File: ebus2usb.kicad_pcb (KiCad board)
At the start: 2 copper layers, 86.8 x 30.4 mm, 42 parts, among them J1 MKDSN1,5/2-5,08, J2 Molex 53047-0210, J3 Molex 53047-0410, J4 Molex 53047-0210, J5 Molex 53047-0410, J6 Molex 67068-8000, Q1 BC817-40, Q2 BC817-40, U1 TS3702, U2 ADuM1201, U3 CH340N

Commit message: v0.8.1 * Size of main board changed to 87mm x 14.8mm * R5 changed from 1K5 to 4K7 * TS3702/TCL3702 replaced by TSX3702 (need VCC on one input)
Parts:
- R5: value 1K5 -> 4K7
- U1: value TS3702 -> TSX3702
- moved D6 0.20 mm to (113.5, 90.6)
- moved D7 0.20 mm to (123.5, 90.6)
- moved D8 0.20 mm to (133.5, 90.6)
- moved J4 0.20 mm to (104.3, 90.6)
- moved J5 0.20 mm to (137.5, 90.6)
- moved R10 0.20 mm to (123.0, 86.6)
- moved R11 0.20 mm to (133.0, 86.6)
- moved R9 0.20 mm to (113.5, 86.6)
- moved mouse-bite-2mm-slot 0.20 mm to (134.8, 98.6)
- moved mouse-bite-2mm-slot 0.20 mm to (116.2, 98.6)
- moved mouse-bite-2mm-slot 0.20 mm to (107.0, 98.6)
- moved mouse-bite-2mm-slot 0.20 mm to (125.5, 98.6)
- moved J6 0.20 mm to (174.0, 107.0)
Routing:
- net /5V: track 39.4 -> 39.9 mm
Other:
- board size 86.8 x 30.4 mm -> 87 x 30.8 mm

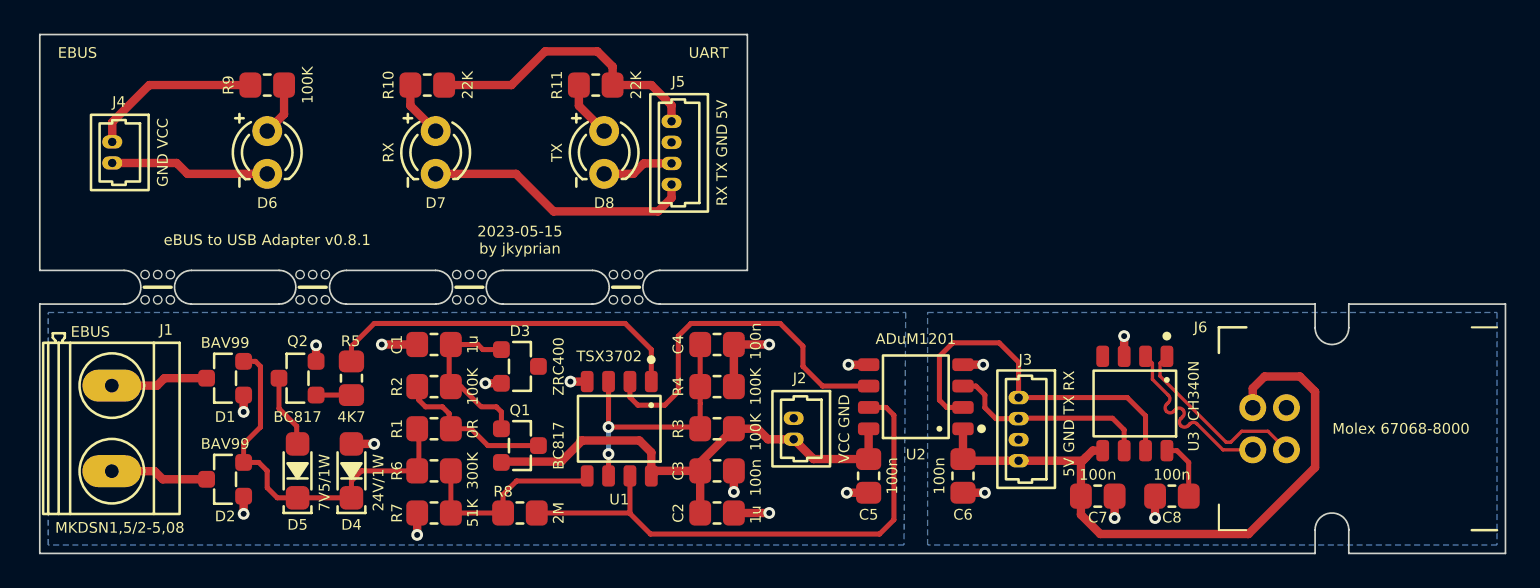
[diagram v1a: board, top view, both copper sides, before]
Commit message: * Replaced voltage reference with low IZT 5V6 zener diode (cheaper but increases power consumption on the eBus side by ~200uA) * C2/C4 changed to 10u * R6/R7 adjusted for ~5V VCC * AZV3002 as replacement for TSX3702 * USB Type-B port replaced by Type-C port * ESC protection for USB port * Phoenix Contact MKDSN connector replaced by MSTBA
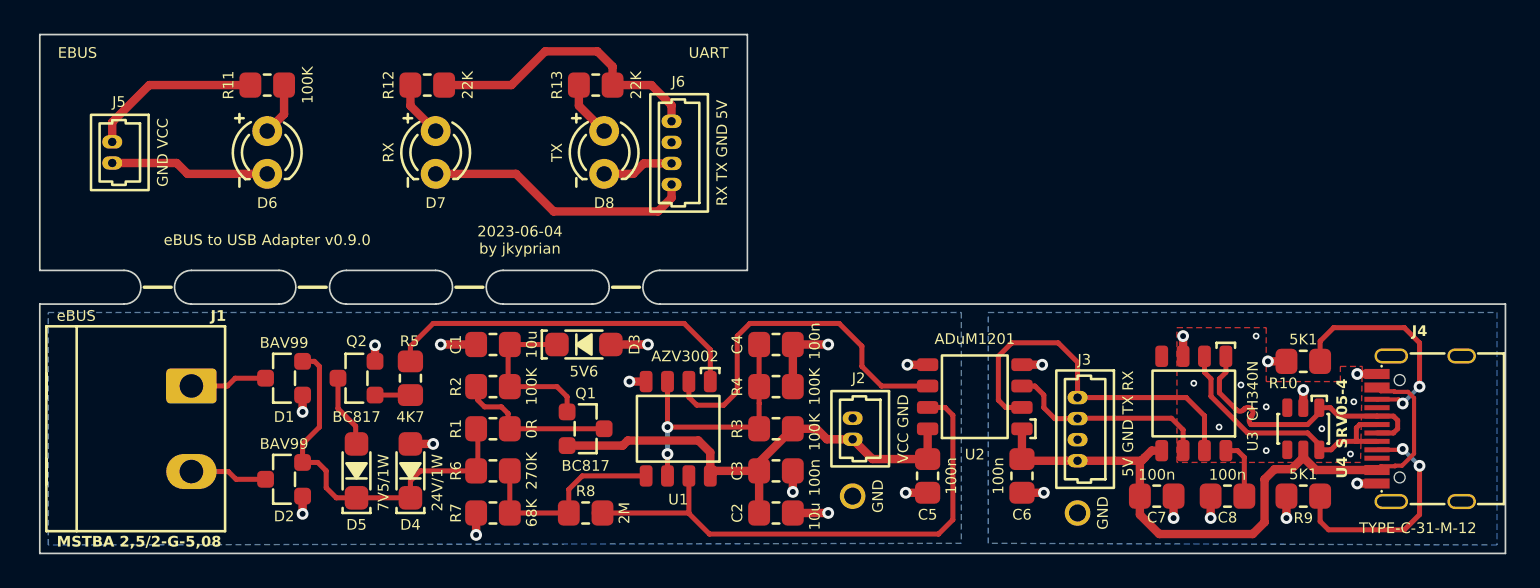
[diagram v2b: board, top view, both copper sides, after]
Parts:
- removed the J6 at (174.0, 107.0)
- removed mouse-bite-2mm-slot (x4): VAL**, ebus2usb:mouse-bite-2mm-slot
- added J4: HRO TYPE-C-31-M-12, ebus2usb:HRO_TYPE-C-31-M-12, F.Cu at (181.9, 107.0)
- added R10: 5K1, ebus2usb:R0805, F.Cu at (175.0, 103.0)
- added R9: 5K1, ebus2usb:R0805, F.Cu at (175.0, 111.0)
- added TP1: Keystone 5021, ebus2usb:Keystone_5021, F.Cu at (148.2, 111.0)
- added TP2: Keystone 5021, ebus2usb:Keystone_5021, F.Cu at (161.6, 112.0)
- added U4: SRV05-4, ebus2usb:SOT-23-6L, F.Cu at (175.0, 107.0)
- C1, C2: value 1u -> 10u
- D3: value ZRC400 -> 5V6; footprint ebus2usb:SOT-23-3 -> ebus2usb:SOD-123
- J1: value MKDSN1,5/2-5,08 -> MSTBA 2,5/2-G-5,08; footprint ebus2usb:MKDSN1,5_2-5,08 -> ebus2usb:MSTBA_2,5_2-G-5,08
- R6: value 300K -> 270K
- R7: value 51K -> 68K
- U1: value TSX3702 -> AZV3002
- moved J1 4.75 mm to (109.0, 107.0)
- moved Q1 4.03 mm to (132.4, 107.0)
- moved D3 4.02 mm to (132.3, 102.0), turned to 0 degrees
- moved R8 3.90 mm to (132.4, 112.0)
- moved C1 3.50 mm to (126.9, 102.0)
- moved C2 3.50 mm to (143.7, 112.0)
- moved C3 3.50 mm to (143.7, 109.5)
- moved C4 3.50 mm to (143.7, 102.0)
- moved C5 3.50 mm to (152.7, 109.8)
- moved C6 3.50 mm to (158.3, 109.8)
- moved C7 3.50 mm to (166.3, 111.0)
- moved D1 3.50 mm to (114.5, 104.0)
- moved D2 3.50 mm to (114.5, 110.0)
- moved D4 3.50 mm to (122.0, 109.5)
- moved D5 3.50 mm to (118.8, 109.5)
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- renumbered J4 to J5, J5 to J6, R9 to R11, R10 to R12, R11 to R13
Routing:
- net Net-(J4-CC1): track 0.00 -> 13.8 mm, vias 0 -> 2
- net Net-(J4-CC2): track 0.00 -> 13.4 mm, vias 0 -> 2
- net /D+: track 11.2 -> 17.2 mm
- net GND1: track 6.30 -> 12.2 mm, vias 5 -> 19
- net /D-: track 11.1 -> 16.2 mm
- net GND2: track 19.9 -> 21.2 mm
- net Net-(J1-Pin_2): track 5.82 -> 4.59 mm
- net Net-(J1-Pin_1): track 5.81 -> 4.59 mm
- net /5V: track 39.9 -> 41.0 mm
- net /VCC: track 30.6 -> 29.7 mm
- added copper zone on F.Cu, net GND1
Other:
- outline, holes or cut-outs redrawn
- board text added: "GND"
- board text added: "TYPE-C-31-M-12"
- board text added: "eBUS"

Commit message: New version with STM32 microcontroller.
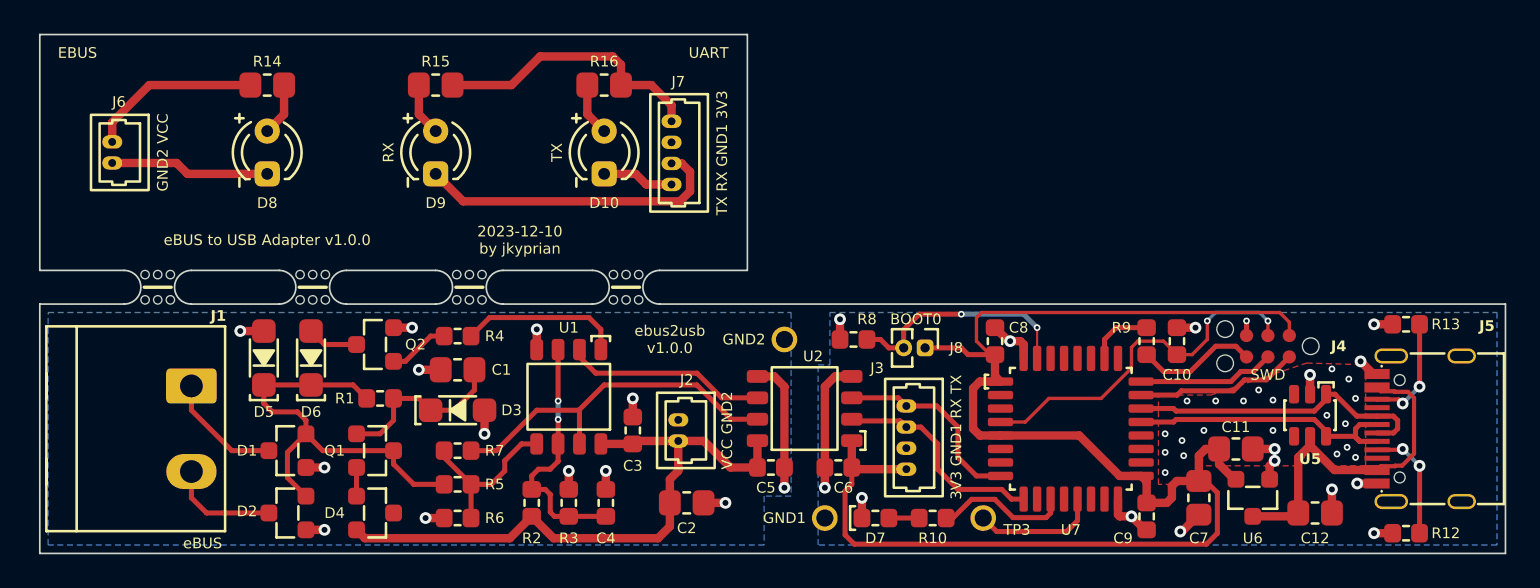
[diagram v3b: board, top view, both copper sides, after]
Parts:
- removed the R1 at (126.9, 107.0)
- removed U3: CH340N, ebus2usb:SO08
- added C10: 100n, ebus2usb:C0603, F.Cu at (167.5, 101.8)
- added C11: 1u, ebus2usb:C0805, F.Cu at (171.0, 108.2)
- added C12: 1u, ebus2usb:C0805, F.Cu at (175.7, 112.0)
- added C9: 100n, ebus2usb:C0603, F.Cu at (165.7, 112.2)
- added D4: BAV99, ebus2usb:SOT-23-3, F.Cu at (119.9, 112.0)
- added D7: LED, ebus2usb:LED_0603, F.Cu at (149.6, 112.3)
- added J4: TC2030, ebus2usb:TC-2030NL, F.Cu at (175.4, 102.1)
- added J8: Harwin M50-3530242, ebus2usb:PinHeader_1x02_P1.27mm, F.Cu at (152.6, 102.2)
- added R10: 47K, ebus2usb:R0603, F.Cu at (153.0, 112.3)
- added R8: 10K, ebus2usb:R0603, F.Cu at (148.3, 101.7)
- added R9: 0R, ebus2usb:R0603, F.Cu at (165.7, 101.8)
- added TP3: Keystone 5021, ebus2usb:Keystone_5021, F.Cu at (156.0, 112.3)
- added U6: XC6206P332MR, ebus2usb:SOT-23-3, F.Cu at (172.0, 111.1)
- added U7: STM32L412KBT6, ebus2usb:LQFP-32, F.Cu at (161.2, 107.0)
- added mouse-bite-2mm-slot: VAL**, ebus2usb:mouse-bite-2mm-slot, F.Cu at (107.0, 98.6)
- added mouse-bite-2mm-slot: VAL**, ebus2usb:mouse-bite-2mm-slot, F.Cu at (116.2, 98.6)
- added mouse-bite-2mm-slot: VAL**, ebus2usb:mouse-bite-2mm-slot, F.Cu at (125.5, 98.6)
- added mouse-bite-2mm-slot: VAL**, ebus2usb:mouse-bite-2mm-slot, F.Cu at (134.8, 98.6)
- C3, C4, C5, C6, C8: footprint ebus2usb:C0805 -> ebus2usb:C0603
- C7: value 100n -> 10u
- R1: renamed from R2; footprint ebus2usb:R0805 -> ebus2usb:R0603
- R12: renamed from R9; footprint ebus2usb:R0805 -> ebus2usb:R0603
- R13: renamed from R10; footprint ebus2usb:R0805 -> ebus2usb:R0603
- R15: renamed from R12; value 22K -> 15K
- R16: renamed from R13; value 22K -> 15K
- R2: renamed from R3; footprint ebus2usb:R0805 -> ebus2usb:R0603
- R3: renamed from R4; footprint ebus2usb:R0805 -> ebus2usb:R0603
- R4: renamed from R5; footprint ebus2usb:R0805 -> ebus2usb:R0603
- R5: renamed from R6; value 270K -> 300K; footprint ebus2usb:R0805 -> ebus2usb:R0603
- R6: renamed from R7; value 68K -> 51K; footprint ebus2usb:R0805 -> ebus2usb:R0603
- R7: renamed from R8; footprint ebus2usb:R0805 -> ebus2usb:R0603
- moved C8 16.6 mm to (156.7, 101.8), turned to 90 degrees
- moved R2 15.2 mm to (129.2, 111.4), turned to -90 degrees
- moved TP2 15.0 mm to (146.6, 112.3)
- moved R3 14.1 mm to (131.4, 111.4), turned to -90 degrees
- moved C4 13.8 mm to (133.6, 111.4), turned to 90 degrees
- moved Q1 12.6 mm to (119.9, 108.3)
- moved D5 11.0 mm to (113.3, 102.8)
- moved C6 10.9 mm to (147.4, 109.3), turned to 0 degrees
- moved J2 10.4 mm to (137.9, 107.1)
- moved J3 10.2 mm to (151.4, 107.5)
- moved TP1 10.1 mm to (144.2, 101.7)
- moved U2 10.1 mm to (145.4, 105.8)
- moved C5 9.31 mm to (143.4, 109.3), turned to 180 degrees
- moved C3 8.83 mm to (135.2, 107.1), turned to 90 degrees
- moved D3 8.45 mm to (124.8, 105.9)
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- renumbered D8 to D10, D4 to D5, D5 to D6, D6 to D8, D7 to D9, J4 to J5, J5 to J6, J6 to J7, R11 to R14, U4 to U5
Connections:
- net /_5V renamed /_3V3
- C6 pad 2: /5V -> /3V3
- C7 pad 1: GND1 -> /3V3
- C7 pad 2: /5V -> GND1
- C8 pad 1: Net-(U3-V3) -> /3V3
- J3 pad 1: /RXD -> /TXD2
- J3 pad 2: /TXD -> /RXD2
- J3 pad 4: /5V -> /3V3
- J7 pad 3: /_TXD -> /_RXD
- J7 pad 4: /_RXD -> /_TXD
- Q1 pad 2: /VCC -> Net-(Q1-E)
- Q1 pad 3: Net-(Q1-C) -> /EBUS
- R1 pad 2: Net-(Q1-C) -> /EBUS
- U2 pad 1: /5V -> /3V3
- U2 pad 2: /RXD -> /RXD2
- U2 pad 3: /TXD -> /TXD2
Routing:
- net /3V3: track 0.00 -> 90.3 mm
- net /RXD: track 21.8 -> 0.00 mm
- net /NRST: track 0.00 -> 21.7 mm, vias 0 -> 2
- net /5V: track 41.0 -> 21.2 mm
- net GND1: track 12.2 -> 29.6 mm, vias 19 -> 36
- net /BOOT0: track 0.00 -> 13.9 mm, vias 0 -> 2
- net /RXD2: track 0.00 -> 13.0 mm
- net /TXD: track 12.3 -> 0.00 mm
- net Net-(R4-Pad2): track 21.9 -> 9.65 mm
- net /TXD2: track 0.00 -> 11.8 mm
- net /VIA: track 32.3 -> 21.5 mm
- net /VOB: track 21.5 -> 12.0 mm
- net Net-(Q1-C): track 9.43 -> 0.00 mm
- net /SWDIO: track 0.00 -> 8.93 mm
- net /LED_GREEN: track 0.00 -> 8.35 mm
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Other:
- board text added: "3V3 GND1 RX TX"
- board text added: "BOOT0"
- board text added: "GND1"
- board text added: "GND2"
- board text added: "GND2 VCC"
- board text added: "SWD"
- board text added: "TX RX GND1 3V3"
- board text added: "VCC GND2"
- board text added: "ebus2usb ${REVISION}"
- board text removed: "5V GND TX RX"
- board text removed: "BC817"
- board text removed: "GND"
- board text removed: "GND VCC"
- board text removed: "JLCJLCJLCJLC"
- board text removed: "RX TX GND 5V"
- board text removed: "VCC GND"
